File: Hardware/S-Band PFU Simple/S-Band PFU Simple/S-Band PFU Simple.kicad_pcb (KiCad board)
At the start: 4 copper layers, 43.2 x 43.2 mm, 16 parts, among them J1 2057-RF2-152-T-00-50-G-HDW-ND, J2 2057-RF2-152-T-00-50-G-HDW-ND, J3 2057-RF2-152-T-00-50-G-HDW-ND, J4 Conn_01x02_Pin, U1 SKY13347-360LF, U2 AZ1117-3.3

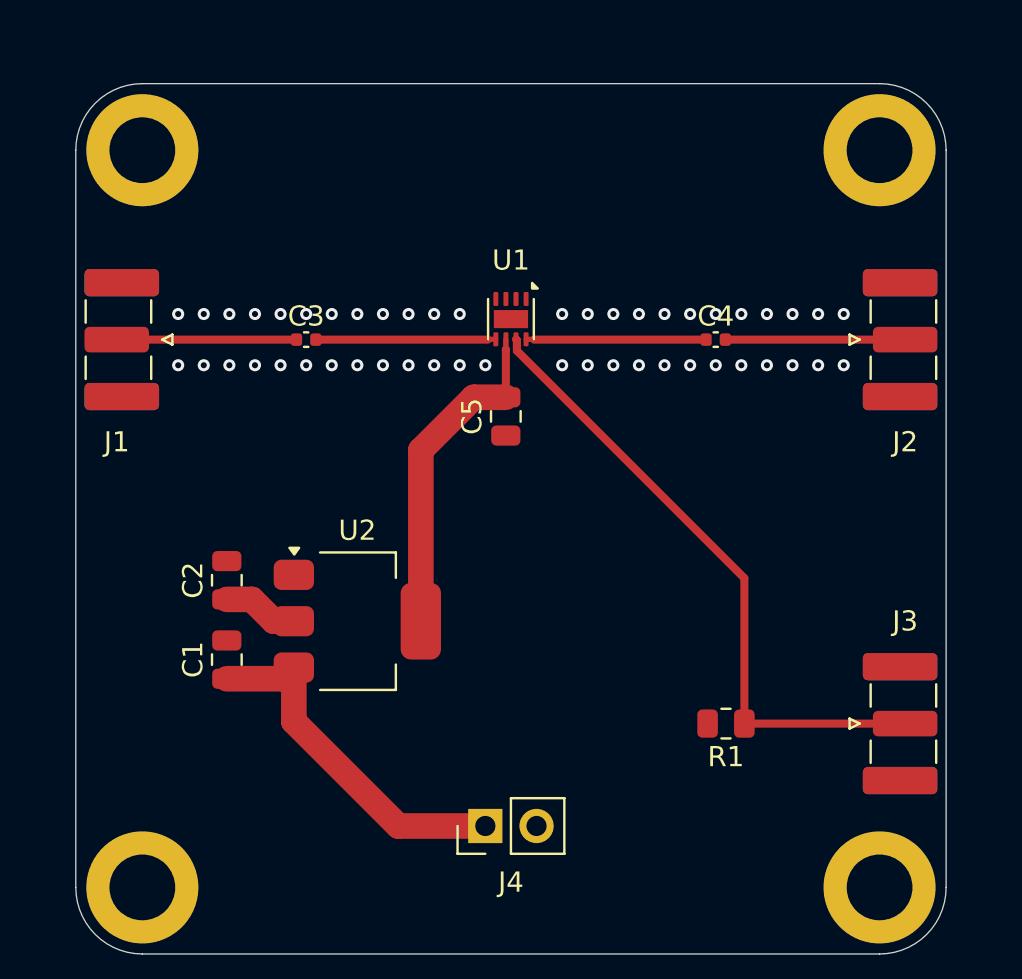
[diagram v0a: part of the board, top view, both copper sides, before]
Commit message: Generating Gerbers for PFU
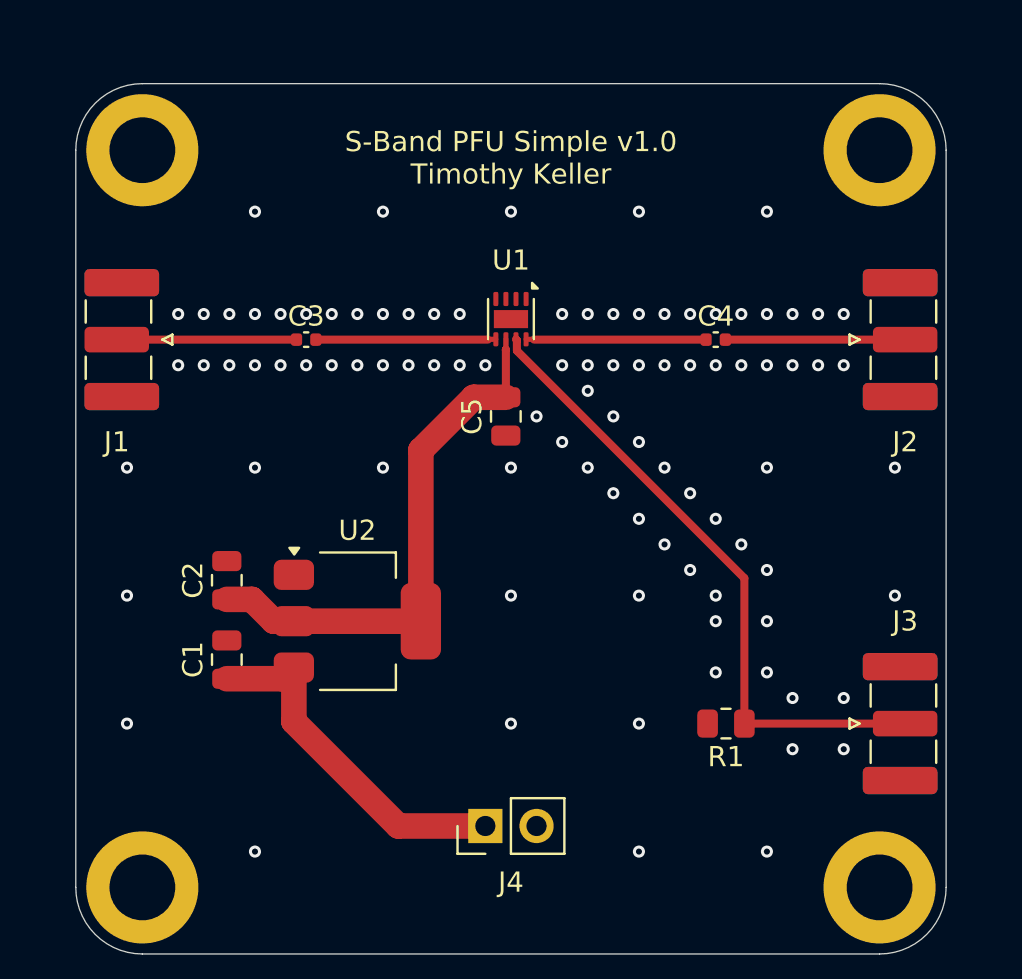
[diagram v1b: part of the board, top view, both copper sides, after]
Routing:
- net +3V3: track 20.4 -> 26.7 mm
- net GND: vias 49 -> 94
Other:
- board text added: "${TITLE} ${REVISION} ${COMMENT1}"

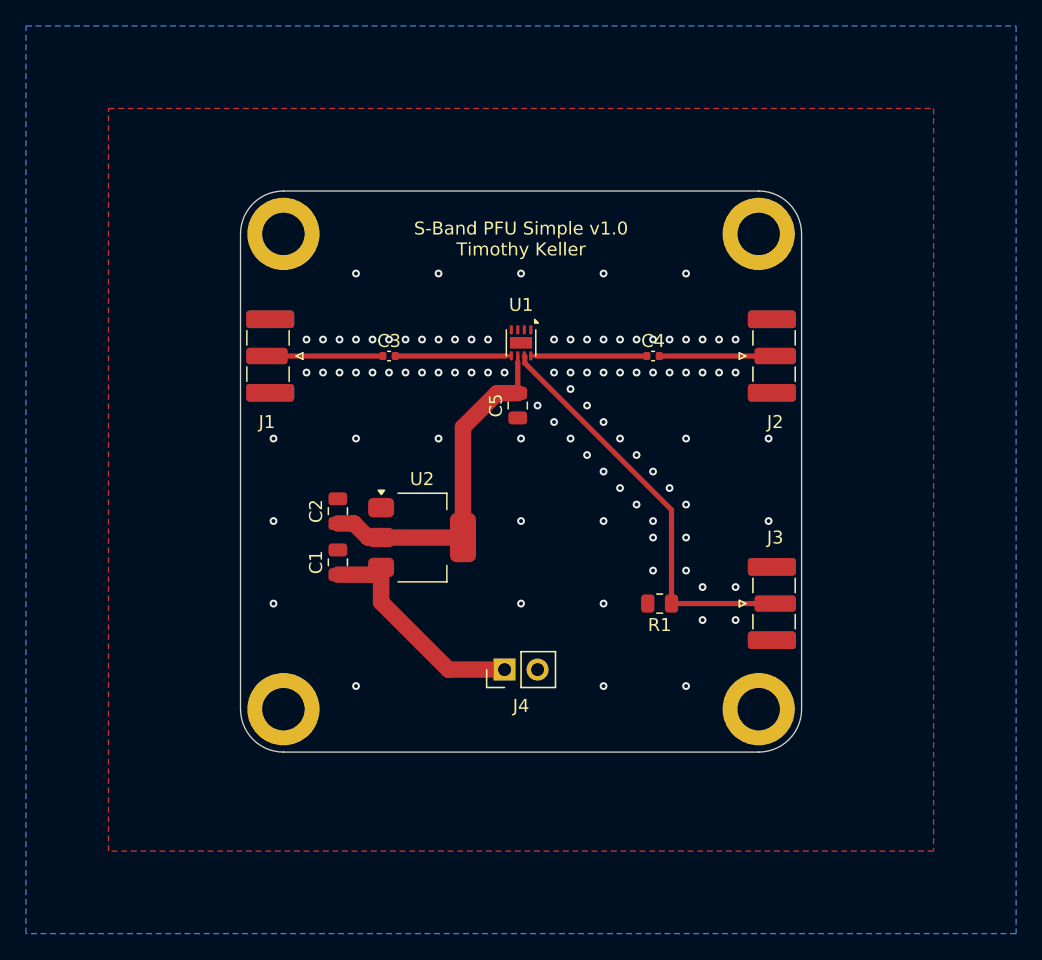
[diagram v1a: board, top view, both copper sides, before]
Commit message: fixed switch
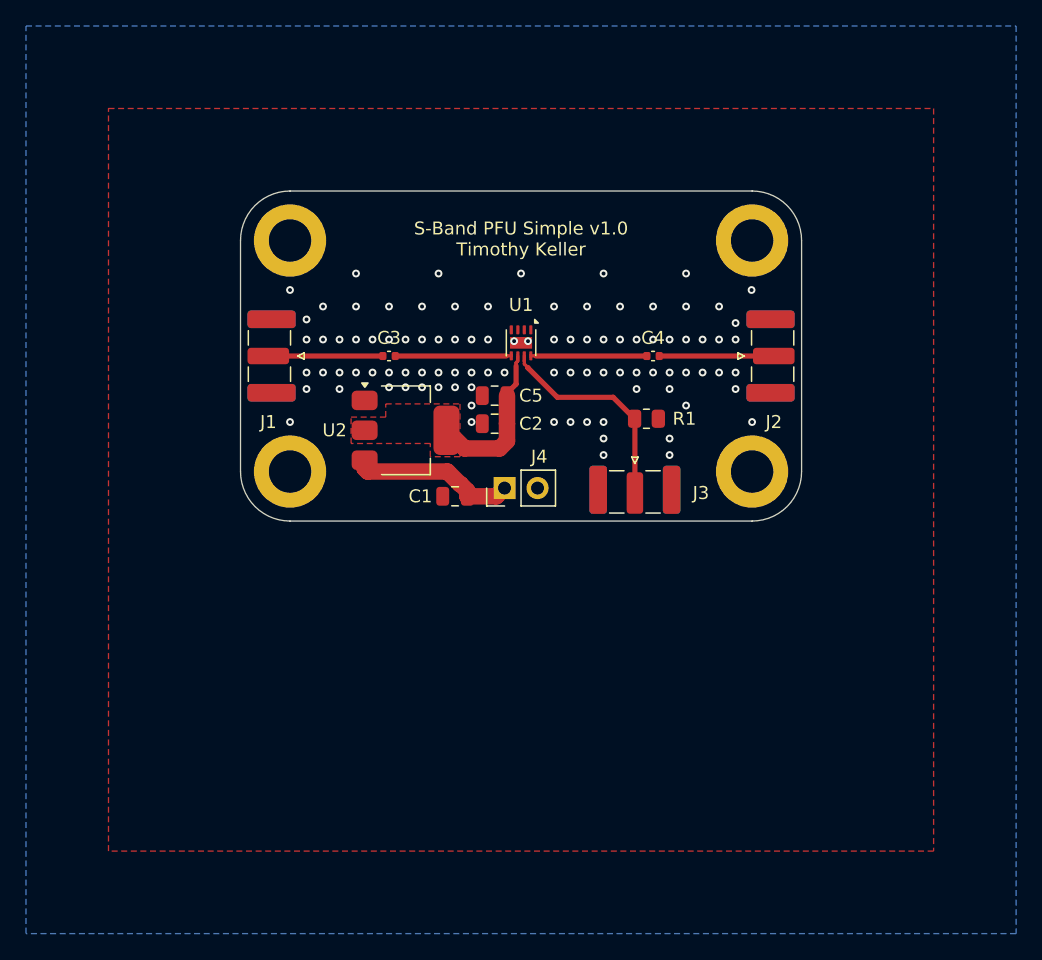
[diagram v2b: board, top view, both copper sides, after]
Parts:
- J4: value Conn_01x02_Pin -> 61300211121
- moved H3 18.3 mm to (113.0, 59.7)
- moved H4 18.3 mm to (77.5, 59.7)
- moved R1 14.3 mm to (104.9, 55.6), turned to 0 degrees
- moved J4 14.0 mm to (94.0, 61.0)
- moved C2 13.8 mm to (93.2, 56.0), turned to 180 degrees
- moved J3 13.7 mm to (104.0, 61.3), turned to -90 degrees
- moved C1 10.3 mm to (90.2, 61.6), turned to 180 degrees
- moved U2 8.35 mm to (86.4, 56.5)
- moved C5 1.93 mm to (93.2, 53.8), turned to 0 degrees
- moved H1 0.72 mm to (77.5, 41.9)
- moved H2 0.72 mm to (113.0, 41.9)
- moved J1 0.11 mm to (75.8, 50.8)
- moved J2 0.11 mm to (114.7, 50.8)
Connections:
- U1 pad 1: unconnected-(U1-NC-Pad1) -> GND
- U1 pad 4: unconnected-(U1-NC-Pad4) -> GND
- U1 pad 9: (no net) -> GND
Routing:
- net GATE: track 31.7 -> 16.6 mm
- net +3V3: track 26.7 -> 12.4 mm
- net +5V: track 17.9 -> 12.8 mm
- net GND: vias 94 -> 96
- added copper zone on F.Cu, net +3V3
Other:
- board size 43.2 x 43.2 mm -> 43.2 x 25.4 mm

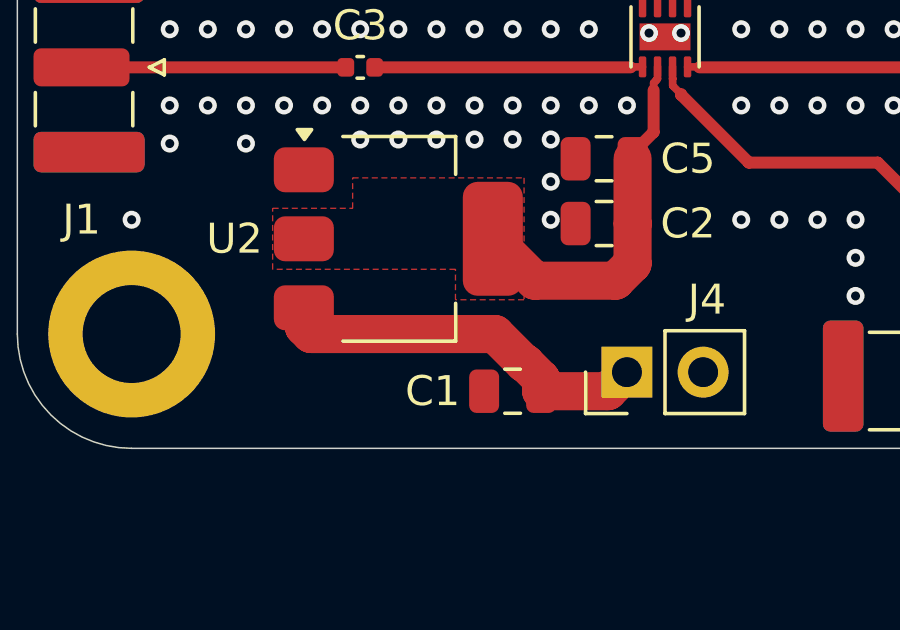
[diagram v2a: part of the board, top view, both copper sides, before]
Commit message: Adding gerbers and bom for gate driver
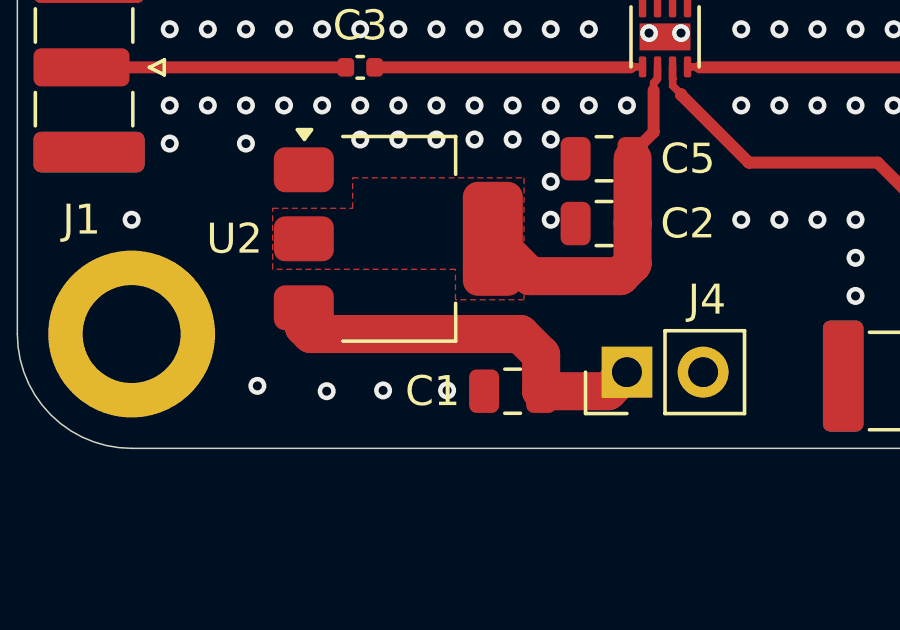
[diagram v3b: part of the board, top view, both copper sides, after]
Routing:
- net GND: vias 96 -> 100
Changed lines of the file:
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@@
 	(title_block
 		(title "S-Band PFU Simple")
-		(date "2025-07-06")
+		(date "2025-07-11")
 		(rev "v1.0")
 		(company "openEPR")
@@
 			(psa4output no)
 			(plot_black_and_white yes)
-			(plotinvisibletext no)
 			(sketchpadsonfab no)
 			(plotpadnumbers no)
@@
 			(drillshape 0)
 			(scaleselection 1)
-			(outputdirectory "${PROJECTNAME}_${REVISION}_Gerbers/")
+			(outputdirectory "${PROJECTNAME}_${REVISION}_Gerbers")
 		)
 	)
@@
 	)
 	(segment
-		(start 91.12 61.189476)
-		(end 91.12 61.595)
+		(start 83.45 59.69)
+		(end 90.424 59.69)
 		(width 1.27)
 		(layer "F.Cu")
@@
 	)
 	(segment
-		(start 90.556 60.663238)
-		(end 90.593762 60.663238)
-		(width 1.27)
-		(layer "F.Cu")
-		(net 1)
-	)
-	(segment
-		(start 90.593762 60.663238)
-		(end 91.12 61.189476)
-		(width 1.27)
-		(layer "F.Cu")
-		(net 1)
-	)
-	(segment
 		(start 83.21 58.815)
 		(end 83.21 59.45)
@@
 	)
 	(segment
-		(start 89.582762 59.69)
-		(end 90.556 60.663238)
+		(start 91.12 60.386)
+		(end 91.12 61.595)
 		(width 1.27)
 		(layer "F.Cu")
@@
 	)
 	(segment
-		(start 83.45 59.69)
-		(end 89.582762 59.69)
+		(start 91.12 61.595)
+		(end 93.345 61.595)
 		(width 1.27)
 		(layer "F.Cu")
@@
 	)
 	(segment
-		(start 91.12 61.595)
-		(end 93.345 61.595)
+		(start 93.345 61.595)
+		(end 93.98 60.96)
 		(width 1.27)
 		(layer "F.Cu")
@@
 	)
 	(segment
-		(start 93.345 61.595)
-		(end 93.98 60.96)
+		(start 90.424 59.69)
+		(end 91.12 60.386)
 		(width 1.27)
 		(layer "F.Cu")
@@
 	)
 	(via
+		(at 87.9856 61.5696)
+		(size 0.6)
+		(drill 0.3)
+		(layers "F.Cu" "B.Cu")
+		(free yes)
+		(net 2)
+	)
+	(via
 		(at 78.74 53.34)
 		(size 0.6)
@@
 	)
 	(via
+		(at 83.9724 61.595)
+		(size 0.6)
+		(drill 0.3)
+		(layers "F.Cu" "B.Cu")
+		(free yes)
+		(net 2)
+	)
+	(via
 		(at 109.22 49.53)
 		(size 0.6)
@@
 	)
 	(via
+		(at 81.661 61.4172)
+		(size 0.6)
+		(drill 0.3)
+		(layers "F.Cu" "B.Cu")
+		(free yes)
+		(net 2)
+	)
+	(via
 		(at 91.44 49.53)
 		(size 0.6)
@@
 	)
 	(via
+		(at 85.852 61.5696)
+		(size 0.6)
+		(drill 0.3)
+		(layers "F.Cu" "B.Cu")
+		(free yes)
+		(net 2)
+	)
+	(via
 		(at 106.68 52.07)
 		(size 0.6)
@@
 	)
 	(segment
+		(start 93.7514 57.7596)
+		(end 94.168 57.343)
+		(width 1.27)
+		(layer "F.Cu")
+		(net 3)
+	)
+	(segment
 		(start 94.869 51.318984)
 		(end 94.953 51.234984)
@@
 	)
 	(segment
-		(start 93.599 57.912)
-		(end 94.168 57.343)
+		(start 94.168 57.343)
+		(end 94.168 56.007)
 		(width 1.27)
 		(layer "F.Cu")
@@
 	)
 	(segment
-		(start 89.51 56.515)
-		(end 90.907 57.912)
+		(start 94.168 56.007)
+		(end 94.168 53.848)
 		(width 1.27)
 		(layer "F.Cu")
@@
 	)
 	(segment
-		(start 94.168 56.007)
-		(end 94.168 53.848)
+		(start 89.51 56.515)
+		(end 90.7546 57.7596)
 		(width 1.27)
 		(layer "F.Cu")
@@
 	)
 	(segment
-		(start 94.168 57.343)
-		(end 94.168 56.007)
+		(start 90.7546 57.7596)
+		(end 93.7514 57.7596)
 		(width 1.27)
 		(layer "F.Cu")
@@
 		(layer "F.Cu")
 		(net 3)
-	)
-	(segment
-		(start 90.907 57.912)
-		(end 93.599 57.912)
-		(width 1.27)
-		(layer "F.Cu")
-		(net 3)
